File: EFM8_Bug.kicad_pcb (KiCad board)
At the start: 2 copper layers, 29.4 x 10.2 mm, 11 parts, among them J1 USB_C_Receptacle_USB2.0, P1 C2 Debug interface, P2 CONN_9, P3 CONN_9, U1 MCP1703A-3302_SOT23, U2 EFM8BB10F8G-A-QFN20

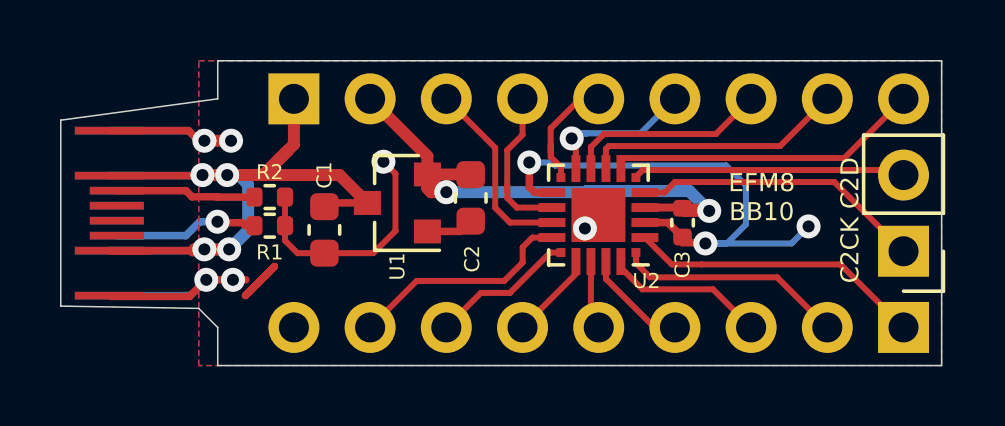
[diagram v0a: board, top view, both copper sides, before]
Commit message: LDO and fuse selected
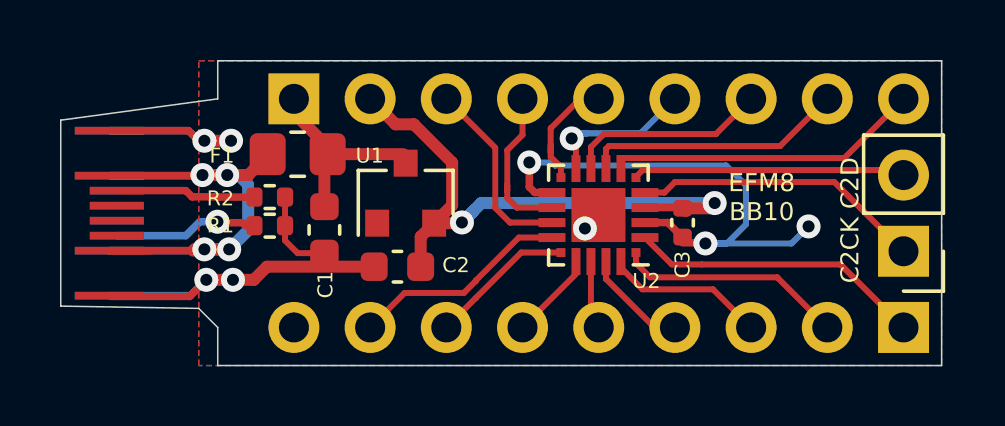
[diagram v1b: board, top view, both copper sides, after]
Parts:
- added F1: SR075-06, Resistor_SMD:R_0805_2012Metric_Pad1.20x1.40mm_HandSolder, F.Cu at (76.3, 83.1)
- C1: value C_Small -> 1uF
- C2: value C_Small -> 2.2uF
- U1: value MCP1703A-3302_SOT23 -> AP2210-3.3TRG1
- moved C2 3.35 mm to (79.7, 86.9), turned to 180 degrees
- moved U1 0.43 mm to (79.9, 84.4), turned to 90 degrees
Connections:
- J1 pad A4: VBUS -> Net-(F1-Pad2)
- J1 pad A9: VBUS -> Net-(F1-Pad2)
- J1 pad B4: VBUS -> Net-(F1-Pad2)
- J1 pad B9: VBUS -> Net-(F1-Pad2)
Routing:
- net VBUS: track 41.6 -> 6.94 mm, vias 4 -> 0
- net Net-(F1-Pad2): track 0.00 -> 27.0 mm, vias 0 -> 4
- net GND: track 48.7 -> 45.1 mm, vias 9 -> 8

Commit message: USB-C receptacle in pcb layout drafted
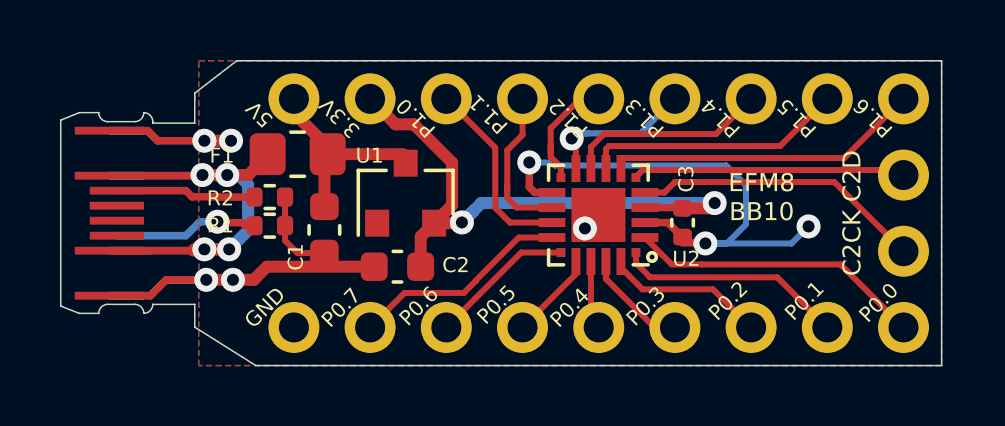
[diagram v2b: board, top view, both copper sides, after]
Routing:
- net GND: track 45.1 -> 45.9 mm
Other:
- outline, holes or cut-outs redrawn
- board text added: "1.6"
- board text added: "3.3V"
- board text added: "5V"
- board text added: "C2CK"
- board text added: "C2D"
- board text added: "GND"
- board text added: "P0.0"
- board text added: "P0.1"
- board text added: "P0.2"
- board text added: "P0.3"
- board text added: "P0.4"
- board text added: "P0.5"
- board text added: "P0.6"
- board text added: "P0.7"
- board text added: "P1.0"
- board text added: "P1.1"
- board text added: "P1.2"
- board text added: "P1.3"
- board text added: "P1.4"
- board text added: "P1.5"
- board text added: "P1.6"
- board text added: "USB-C PWR only"

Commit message: Depopulated unused lines from cursed USB-C connector
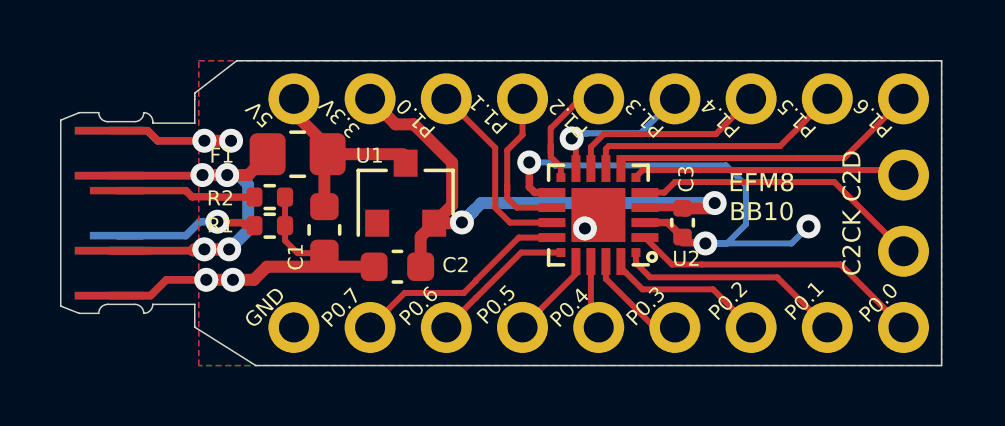
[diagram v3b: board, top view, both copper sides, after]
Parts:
- J1: footprint EFM8_Bug:usb-c-depopulated-2.0-pcb -> EFM8_Bug:usb-c-depopulated-2.0-power-only-pcb

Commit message: Generated IBOM
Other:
- board text removed: "C2CK C2D"
